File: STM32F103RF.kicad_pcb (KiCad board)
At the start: 4 copper layers, 68 x 24 mm, 56 parts, among them J1 USB_C_Receptacle_USB2.0, J2 Conn_01x04, J3 Conn_Coaxial, U1 SPX3819M5-L-3-3, U2 STM32F103C6Tx, U3 NRF24L01, Y1 16MHz, Y2 16MHz

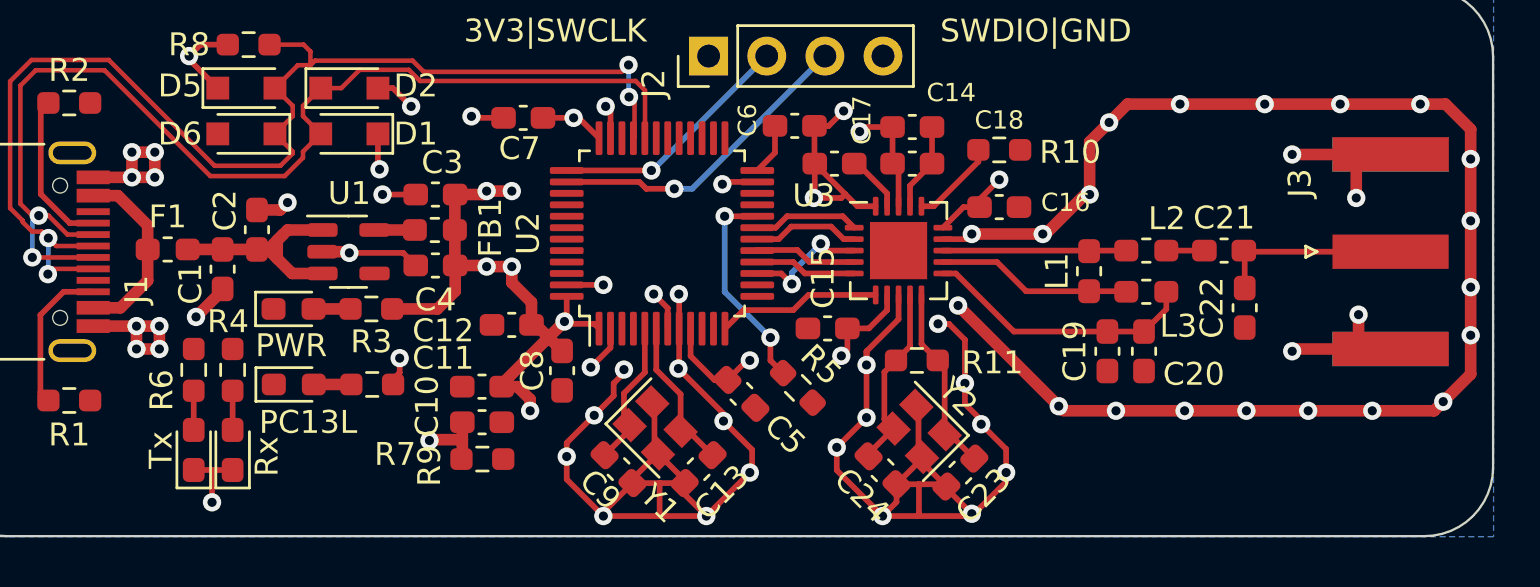
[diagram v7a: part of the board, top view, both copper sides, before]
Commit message: removed sma connector -> wrong footprint
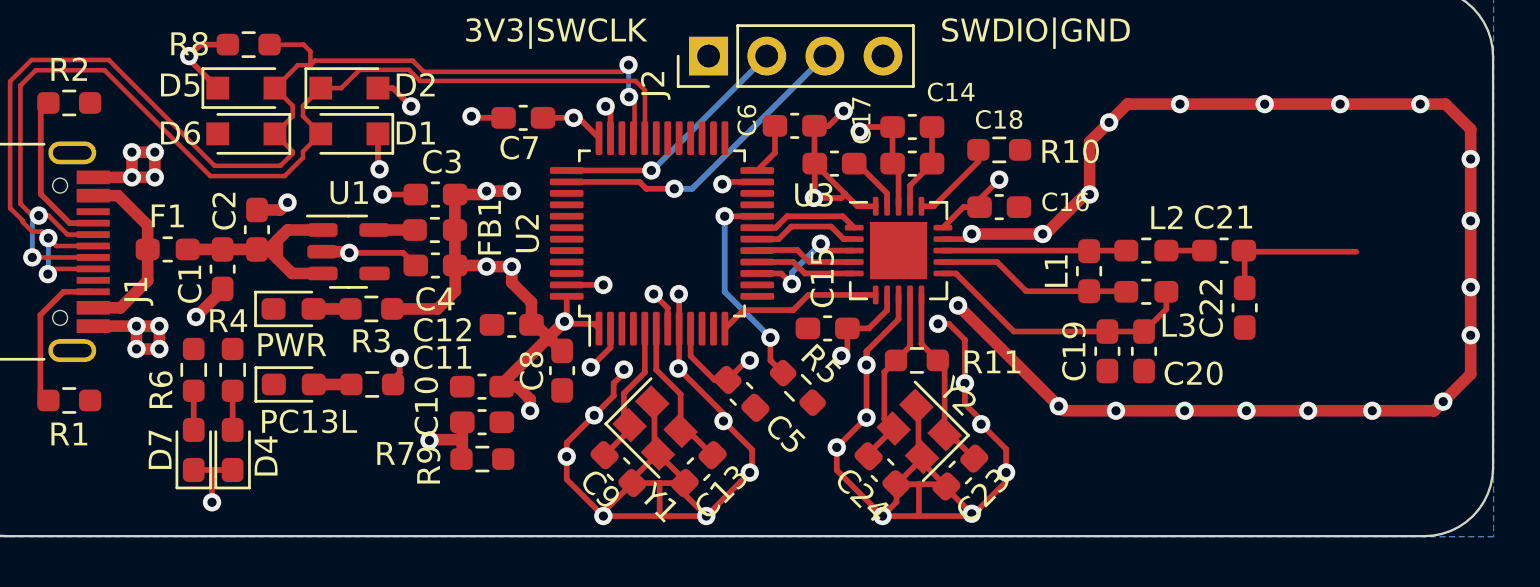
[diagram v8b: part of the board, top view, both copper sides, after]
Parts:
- removed J3: Conn_Coaxial, Connector_Coaxial:SMA_Amphenol_132289_EdgeMount
- renumbered Rx to D4, Tx to D7
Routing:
- net GND: track 194.2 -> 185.1 mm, vias 62 -> 58
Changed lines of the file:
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@@
     (property "Sheetname" "Microcontroller")
     (attr smd)
-    (fp_text reference "Rx" (at -0.2875 1.5 90) (layer "F.SilkS")
+    (fp_text reference "D4" (at -0.2875 1.5 90) (layer "F.SilkS")
       (effects (font (size 1 1) (thickness 0.15)))
     )
@@
     )
   )
-  (footprint "Connector_Coaxial:SMA_Amphenol_132289_EdgeMount" (layer "F.Cu")
-    (at 99.5 30.55)
-    (descr "http://www.amphenolrf.com/132289.html")
-    (tags "SMA")
-    (property "Sheetfile" "NRF24L01.kicad_sch")
-    (property "Sheetname" "NRF24L01")
-    (attr smd)
-    (fp_text reference "J3" (at -3.96 -3 90) (layer "F.SilkS")
-      (effects (font (size 1 1) (thickness 0.15)))
-    )
-    (fp_text value "Conn_Coaxial" (at 5 6) (layer "F.Fab")
-      (effects (font (size 1 1) (thickness 0.15)))
-    )
-    (fp_text user "${REFERENCE}" (at 4.79 0 90) (layer "F.Fab")
-      (effects (font (size 1 1) (thickness 0.15)))
-    )
-    (fp_line (start -3.71 0.25) (end -3.21 0) (layer "F.SilkS") (width 0.12))
-    (fp_line (start -3.71 -0.25) (end -3.71 0.25) (layer "F.SilkS") (width 0.12))
-    (fp_line (start -3.21 0) (end -3.71 -0.25) (layer "F.SilkS") (width 0.12))
-    (fp_line (start 14.47 -5.58) (end -3.04 -5.58) (layer "B.CrtYd") (width 0.05))
-    (fp_line (start 14.47 -5.58) (end 14.47 5.58) (layer "B.CrtYd") (width 0.05))
-    (fp_line (start -3.04 5.58) (end -3.04 -5.58) (layer "B.CrtYd") (width 0.05))
-    (fp_line (start 14.47 5.58) (end -3.04 5.58) (layer "B.CrtYd") (width 0.05))
-    (fp_line (start 14.47 5.58) (end -3.04 5.58) (layer "F.CrtYd") (width 0.05))
-    (fp_line (start 14.47 -5.58) (end -3.04 -5.58) (layer "F.CrtYd") (width 0.05))
-    (fp_line (start 14.47 -5.58) (end 14.47 5.58) (layer "F.CrtYd") (width 0.05))
-    (fp_line (start -3.04 5.58) (end -3.04 -5.58) (layer "F.CrtYd") (width 0.05))
-    (fp_line (start 4.445 -3.81) (end 4.445 -5.08) (layer "F.Fab") (width 0.1))
-    (fp_line (start -1.91 5.08) (end 4.445 5.08) (layer "F.Fab") (width 0.1))
-    (fp_line (start -1.91 3.81) (end -1.91 5.08) (layer "F.Fab") (width 0.1))
-    (fp_line (start -1.91 -3.81) (end 2.54 -3.81) (layer "F.Fab") (width 0.1))
-    (fp_line (start 2.54 3.81) (end -1.91 3.81) (layer "F.Fab") (width 0.1))
-    (fp_line (start 4.445 5.08) (end 4.445 3.81) (layer "F.Fab") (width 0.1))
-    (fp_line (start 2.54 -3.81) (end 2.54 3.81) (layer "F.Fab") (width 0.1))
-    (fp_line (start 13.97 -3.81) (end 13.97 3.81) (layer "F.Fab") (width 0.1))
-    (fp_line (start 3.54 0) (end 2.54 0.75) (layer "F.Fab") (width 0.1))
-    (fp_line (start -1.91 -5.08) (end 4.445 -5.08) (layer "F.Fab") (width 0.1))
-    (fp_line (start -1.91 -5.08) (end -1.91 -3.81) (layer "F.Fab") (width 0.1))
-    (fp_line (start 4.445 -3.81) (end 13.97 -3.81) (layer "F.Fab") (width 0.1))
-    (fp_line (start 13.97 3.81) (end 4.445 3.81) (layer "F.Fab") (width 0.1))
-    (fp_line (start 2.54 -0.75) (end 3.54 0) (layer "F.Fab") (width 0.1))
-    (pad "1" smd rect (at 0 0 90) (size 1.5 5.08) (layers "F.Cu" "F.Paste" "F.Mask")
-      (net 54 "Net-(C21-Pad2)") (pinfunction "In") (pintype "passive"))
-    (pad "2" smd rect (at 0 4.25 90) (size 1.5 5.08) (layers "F.Cu" "F.Paste" "F.Mask")
-      (net 1 "GND") (pinfunction "Ext") (pintype "passive"))
-    (pad "2" smd rect (at 0 4.25 90) (size 1.5 5.08) (layers "B.Cu" "B.Paste" "B.Mask")
-      (net 1 "GND") (pinfunction "Ext") (pintype "passive"))
-    (pad "2" smd rect (at 0 -4.25 90) (size 1.5 5.08) (layers "F.Cu" "F.Paste" "F.Mask")
-      (net 1 "GND") (pinfunction "Ext") (pintype "passive"))
-    (pad "2" smd rect (at 0 -4.25 90) (size 1.5 5.08) (layers "B.Cu" "B.Paste" "B.Mask")
-      (net 1 "GND") (pinfunction "Ext") (pintype "passive"))
-    (model "${KICAD6_3DMODEL_DIR}/Connector_Coaxial.3dshapes/SMA_Amphenol_132289_EdgeMount.wrl"
-      (offset (xyz 0 0 0))
-      (scale (xyz 1 1 1))
-      (rotate (xyz 0 0 0))
-    )
-  )
   (footprint "LED_SMD:LED_0603_1608Metric_Pad1.05x0.95mm_HandSolder" (layer "F.Cu")
     (at 47.2 39.2125 90)
@@
     (property "Sheetname" "Microcontroller")
     (attr smd)
-    (fp_text reference "Tx" (at 0 -1.43 90) (layer "F.SilkS")
+    (fp_text reference "D7" (at 0 -1.43 90) (layer "F.SilkS")
       (effects (font (size 1 1) (thickness 0.15)))
     )
@@
   (segment (start 85.2 37.5) (end 87.5 37.5) (width 0.508) (layer "F.Cu") (net 1))
   (segment (start 78.89012 40.70988) (end 78.89012 41.99012) (width 0.25) (layer "F.Cu") (net 1))
-  (segment (start 95.3 34.8) (end 95.2 34.9) (width 0.508) (layer "F.Cu") (net 1))
   (segment (start 71.825 27.5) (end 70.4 27.5) (width 0.25) (layer "F.Cu") (net 1))
   (segment (start 52.825 30.55) (end 53.95 30.55) (width 0.508) (layer "F.Cu") (net 1))
@@
   (segment (start 44.7 33.8) (end 44.7 34.8) (width 0.508) (layer "F.Cu") (net 1))
   (segment (start 44.7 33.8) (end 45.7 33.8) (width 0.508) (layer "F.Cu") (net 1))
-  (segment (start 98.1 33.3) (end 98.1 34.8) (width 0.508) (layer "F.Cu") (net 1))
   (segment (start 103 25.2) (end 101.9 24.1) (width 0.508) (layer "F.Cu") (net 1))
   (segment (start 63.5 40.5) (end 65.1 42.1) (width 0.25) (layer "F.Cu") (net 1))
@@
   (segment (start 71.6 40.1) (end 69.6 42.1) (width 0.25) (layer "F.Cu") (net 1))
   (segment (start 65.1 41.93226) (end 66.37238 40.65988) (width 0.25) (layer "F.Cu") (net 1))
-  (segment (start 95.2 26.3) (end 98 26.3) (width 0.508) (layer "F.Cu") (net 1))
   (segment (start 78.776256 37.286307) (end 78.870967 37.381018) (width 0.25) (layer "F.Cu") (net 1))
   (segment (start 71.6 39.2) (end 71.6 40.1) (width 0.25) (layer "F.Cu") (net 1))
@@
   (segment (start 67.55988 42.05988) (end 67.6 42.1) (width 0.25) (layer "F.Cu") (net 1))
   (segment (start 69.6 42.1) (end 67.6 42.1) (width 0.25) (layer "F.Cu") (net 1))
-  (segment (start 98 26.3) (end 98 28.2) (width 0.508) (layer "F.Cu") (net 1))
   (segment (start 55.9 23.4) (end 55.25 23.4) (width 0.25) (layer "F.Cu") (net 1))
   (segment (start 78.870967 39.360916) (end 79.023744 39.513693) (width 0.25) (layer "F.Cu") (net 1))
@@
   (segment (start 56.7 24.2) (end 55.9 23.4) (width 0.25) (layer "F.Cu") (net 1))
   (segment (start 94 24.1) (end 97.3 24.1) (width 0.508) (layer "F.Cu") (net 1))
-  (segment (start 98.1 34.8) (end 95.3 34.8) (width 0.508) (layer "F.Cu") (net 1))
   (segment (start 77.90988 40.70988) (end 77.90988 41.49012) (width 0.25) (layer "F.Cu") (net 1))
   (segment (start 75.6 24.4) (end 74.95 25.05) (width 0.25) (layer "F.Cu") (net 1))
@@
   (via (at 103 29.2) (size 0.8) (drill 0.4) (layers "F.Cu" "B.Cu") (net 1))
   (via (at 45.7 33.8) (size 0.8) (drill 0.4) (layers "F.Cu" "B.Cu") (net 1))
-  (via (at 95.2 26.3) (size 0.8) (drill 0.4) (layers "F.Cu" "B.Cu") (net 1))
-  (via (at 95.2 34.9) (size 0.8) (drill 0.4) (layers "F.Cu" "B.Cu") (net 1))
   (via (at 59.336885 24.63479) (size 0.8) (drill 0.4) (layers "F.Cu" "B.Cu") (net 1))
   (via (at 69.6 42.1) (size 0.8) (drill 0.4) (layers "F.Cu" "B.Cu") (net 1))
@@
   (via (at 64.7 37.7) (size 0.8) (drill 0.4) (layers "F.Cu" "B.Cu") (net 1))
   (via (at 82.7 40.2) (size 0.8) (drill 0.4) (layers "F.Cu" "B.Cu") (net 1))
-  (via (at 98.1 33.3) (size 0.8) (drill 0.4) (layers "F.Cu" "B.Cu") (net 1))
   (via (at 81.2 29.7755) (size 0.8) (drill 0.4) (layers "F.Cu" "B.Cu") (net 1))
   (via (at 44.5 27.3) (size 0.8) (drill 0.4) (layers "F.Cu" "B.Cu") (net 1))
@@
   (via (at 65.2 24.2) (size 0.8) (drill 0.4) (layers "F.Cu" "B.Cu") (net 1))
   (via (at 70.3 27.6) (size 0.8) (drill 0.4) (layers "F.Cu" "B.Cu") (net 1))
-  (via (at 98 28.2) (size 0.8) (drill 0.4) (layers "F.Cu" "B.Cu") (net 1))
   (via (at 68.4 32.4) (size 0.8) (drill 0.4) (layers "F.Cu" "B.Cu") (net 1))
   (via (at 65.1 42.1) (size 0.8) (drill 0.4) (layers "F.Cu" "B.Cu") (net 1))
